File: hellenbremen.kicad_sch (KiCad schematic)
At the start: 10 parts

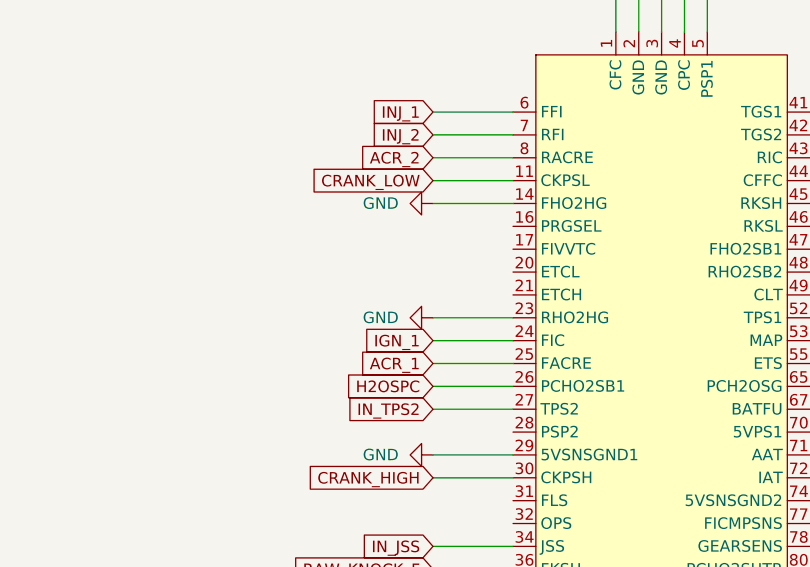
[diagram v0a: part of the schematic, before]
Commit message: adding electronic throttle control
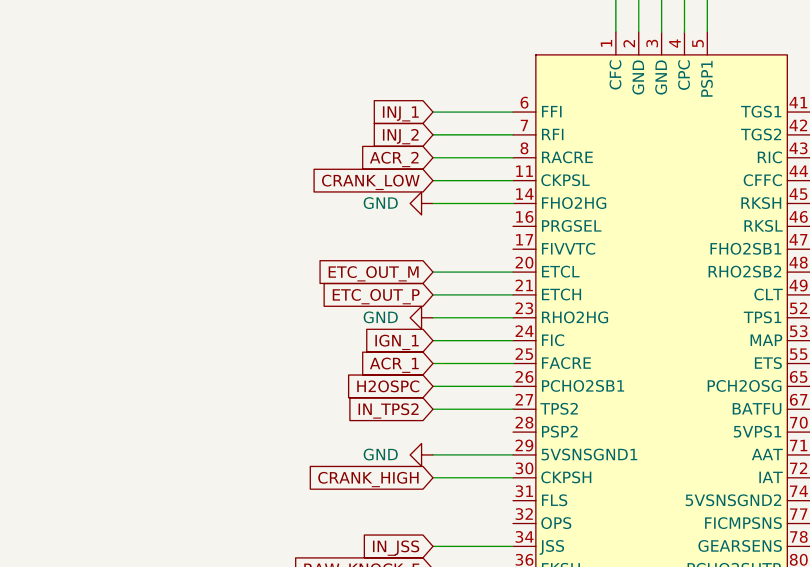
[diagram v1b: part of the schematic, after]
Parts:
- TP1, TP2, TP3, TP4, TP5: now left out of the parts list
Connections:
- net ETC_OUT_M: now reaches J1.20 (ETCL)
- net ETC_OUT_P: now reaches J1.21 (ETCH)
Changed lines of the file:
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@@
+	(wire
+		(pts
+			(xy 102.87 81.28) (xy 111.76 81.28)
+		)
+		(stroke
+			(width 0)
+			(type default)
+		)
+	)
 	(wire
 		(pts
@@
 	(wire
 		(pts
-			(xy 123.19 43.18) (xy 123.19 54.61)
+			(xy 102.87 83.82) (xy 111.76 83.82)
 		)
 		(stroke
@@
 	(wire
 		(pts
-			(xy 144.78 86.36) (xy 153.67 86.36)
+			(xy 123.19 43.18) (xy 123.19 54.61)
 		)
 		(stroke
@@
 	(wire
 		(pts
-			(xy 144.78 78.74) (xy 153.67 78.74)
+			(xy 144.78 86.36) (xy 153.67 86.36)
 		)
 		(stroke
@@
 		)
 	)
+	(wire
+		(pts
+			(xy 144.78 78.74) (xy 153.67 78.74)
+		)
+		(stroke
+			(width 0)
+			(type default)
+		)
+	)
 	(text "Hellen-Bremen"
 		(exclude_from_sim no)
@@
 		)
 	)
+	(global_label "ETC_OUT_M"
+		(shape input)
+		(at 102.87 81.28 180)
+		(fields_autoplaced yes)
+		(effects
+			(font
+				(size 1.27 1.27)
+			)
+			(justify right)
+		)
+		(property "Intersheetrefs" "${INTERSHEET_REFS}"
+			(at 89.483 81.28 0)
+			(effects
+				(font
+					(size 1.27 1.27)
+				)
+				(justify right)
+				(hide yes)
+			)
+		)
+	)
 	(global_label "IN_PPS"
 		(shape input)
@@
 				)
 				(justify left)
+				(hide yes)
+			)
+		)
+	)
+	(global_label "ETC_OUT_P"
+		(shape input)
+		(at 102.87 83.82 180)
+		(fields_autoplaced yes)
+		(effects
+			(font
+				(size 1.27 1.27)
+			)
+			(justify right)
+		)
+		(property "Intersheetrefs" "${INTERSHEET_REFS}"
+			(at 89.6644 83.82 0)
+			(effects
+				(font
+					(size 1.27 1.27)
+				)
+				(justify right)
 				(hide yes)
 			)
@@
 		(exclude_from_sim yes)
 		(in_bom no)
-		(on_board no)
+		(on_board yes)
 		(dnp no)
 		(fields_autoplaced yes)
@@
 		(unit 1)
 		(exclude_from_sim no)
-		(in_bom yes)
+		(in_bom no)
 		(on_board yes)
 		(dnp no)
@@
 		(unit 1)
 		(exclude_from_sim no)
-		(in_bom yes)
+		(in_bom no)
 		(on_board yes)
 		(dnp no)
@@
 		(exclude_from_sim yes)
 		(in_bom no)
-		(on_board no)
+		(on_board yes)
 		(dnp no)
 		(fields_autoplaced yes)
@@
 		(unit 1)
 		(exclude_from_sim no)
-		(in_bom yes)
+		(in_bom no)
 		(on_board yes)
 		(dnp no)
@@
 		(unit 1)
 		(exclude_from_sim no)
-		(in_bom yes)
+		(in_bom no)
 		(on_board yes)
 		(dnp no)
@@
 		(exclude_from_sim yes)
 		(in_bom no)
-		(on_board no)
+		(on_board yes)
 		(dnp no)
 		(fields_autoplaced yes)
@@
 		(exclude_from_sim yes)
 		(in_bom no)
-		(on_board no)
+		(on_board yes)
 		(dnp no)
 		(fields_autoplaced yes)
@@
 		(unit 1)
 		(exclude_from_sim no)
-		(in_bom yes)
+		(in_bom no)
 		(on_board yes)
 		(dnp no)

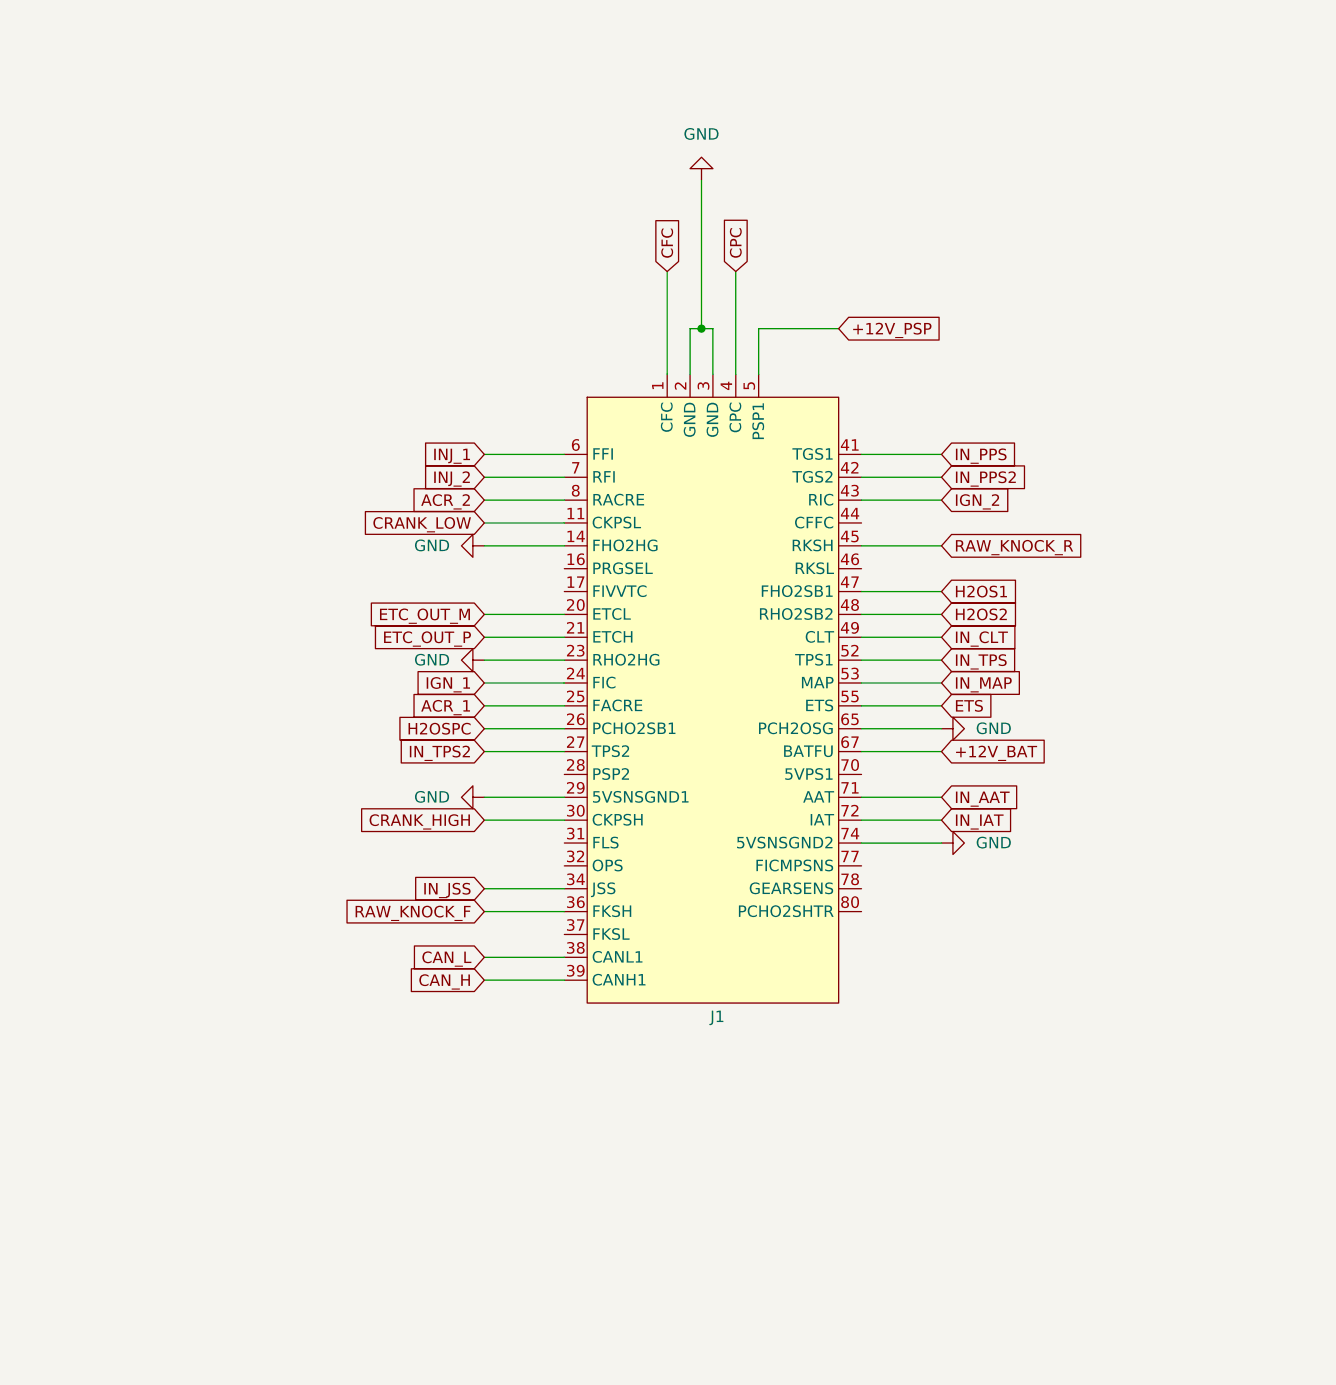
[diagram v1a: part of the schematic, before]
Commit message: adding most remaining outputs and sensors like vvt, cam etc
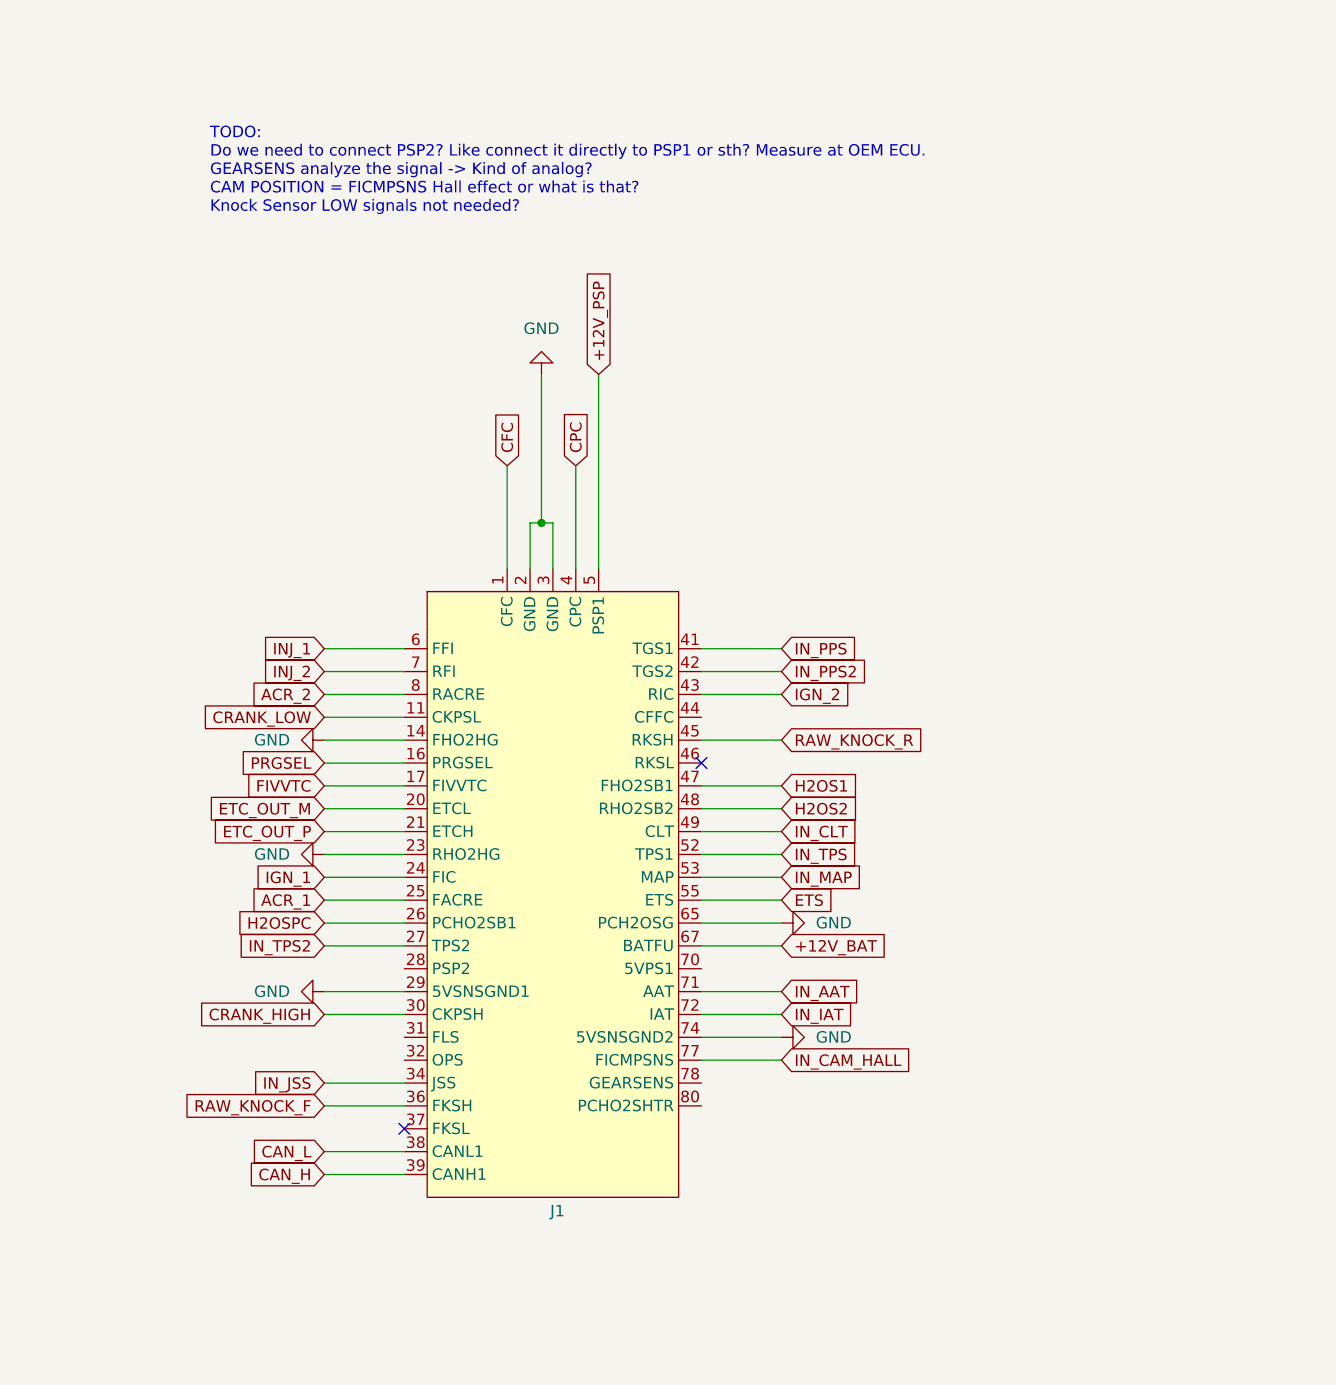
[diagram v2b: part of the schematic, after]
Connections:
- net PRGSEL: now reaches J1.16 (PRGSEL)
- net FIVVTC: now reaches J1.17 (FIVVTC)
- net IN_CAM_HALL: now reaches J1.77 (FICMPSNS)
- no-connect marks 0 -> 2
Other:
- note added: "TODO: Do we need to connect PSP2? Like connect it directly to PSP1 or sth? Measure at OEM ECU. GEARSENS analyze the signal -> Kind of analog? CAM POSITION = FICMPSNS Hall effect or what is that? Knock Sensor LOW signals not needed?"
- moved on the sheet: J1

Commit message: redone layout, possibly feature complete
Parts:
- added M2: Module-power_12and5V-0.2, 0.2:power_12and5V, symbol power_12and5V:Module-power_12and5V-0.2
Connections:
- net +12V: now also M2.E2 (V12)
- net +12V_BAT: now also M2.V1 (V12_PERM)
- net +12V_PSP: now also M2.V2 (IN_VIGN), M2.V3 (V12_RAW)
- net +5V: now also M2.E4 (V5)
- net GND: now also M2.S1 (GND); no longer J1.14 (FHO2HG), J1.23 (RHO2HG)
- net FLS: now reaches J1.31 (FLS)
- net CCFC: now reaches J1.44 (CFFC)
- net GEAR_POS_SENS: now reaches J1.78 (GEARSENS)
- net PCHO2SHTR: now reaches J1.80 (PCHO2SHTR)
- new net +5VP: M2.V4 (5VP)
- new net FHO2H: J1.14 (FHO2HG)
- new net PWR_EN: M2.E5 (EN_5VP)
- new net RHO2H: J1.23 (RHO2HG)
- new net VIGN: M2.E3 (VIGN)
- no-connect marks 2 -> 3
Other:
- removed sheet Power
- note added: "TODO: Do we need to connect PSP2? Like connect it directly to PSP1 or sth? Measure at OEM ECU. DONE: GEARSENS analyze the signal -> Kind of analog? DONE: AM POSITION = FICMPSNS Hall effect or what is that? Knock Sensor LOW signals not needed?"
- note added: "TODO: PSP = IGNITION BASED?"
- note removed: "TODO: Do we need to connect PSP2? Like connect it directly to PSP1 or sth? Measure at OEM ECU. GEARSENS analyze the signal -> Kind of analog? CAM POSITION = FICMPSNS Hall effect or what is that? Knock Sensor LOW signals not needed?"

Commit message: update main connector footprint
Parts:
- J1: footprint HD:TE81PINHD -> HD:HarleyDavidsonDelphi81
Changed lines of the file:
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@@
 			)
 		)
-		(property "Footprint" "HD:TE81PINHD"
+		(property "Footprint" "HD:HarleyDavidsonDelphi81"
 			(at 110.744 88.138 0)
 			(effects
